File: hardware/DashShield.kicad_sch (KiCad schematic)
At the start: 121 parts, among them J001 PWR, J002 Data Logger, J101 CAN0, J202 CAN1, J3 Dash LEDs, J301 Steering Wheel, J601 GPIO, Q301 2N7002, Q302 2N7002, Q303 2N7002, Q501 2N7002, Q502 2N7002, Q503 2N7002, Q504 2N7002, Q505 2N7002, Q506 2N7002, U101 MCP2515-xST, U102 MCP2562-E-SN, U201 MCP2515-xST, U202 MCP2562-E-SN, U401 CAT24C256, U601 ADS1015IDGS, Y101 8MHz, Y201 8MHz

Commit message: feat: added pours & pass-through for CAN0&CAN1
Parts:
- added J102, J203: CAN0, Connector_Molex:Molex_Micro-Fit_3.0_43650-0315_1x03_P3.00mm_Vertical, symbol Connector_Generic:Conn_01x03
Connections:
- net CAN0 High: now also J102.1 (Pin_1)
- net CAN0 Low: now also J102.2 (Pin_2)
- net CAN0 Shield: now also J102.3 (Pin_3)
- net CAN1 High: now also J203.1 (Pin_1)
- net CAN1 Low: now also J203.2 (Pin_2)
- net CAN1 Shield: now also J203.3 (Pin_3)
- net FAST 2: now also J601.33 (Pin_33); no longer J601.32 (Pin_32)
- net FAST LED 0: now also J3.2 (Pin_2); no longer J3.8 (Pin_8)
- net FAST LED 1: now also J3.3 (Pin_3); no longer J3.4 (Pin_4)
- net FAST LED 2: now also J3.4 (Pin_4); no longer J3.3 (Pin_3)
- net GPIO19/PCM.FS: now also Q503.1 (G), R506.1; no longer Q502.1 (G), R504.1
- net GPIO26: now also Q502.1 (G), R504.1; no longer Q501.1 (G), R502.1
- net SLOW LED 1: now also J3.7 (Pin_7); no longer J3.2 (Pin_2)
- net SLOW LED 2: now also J3.8 (Pin_8); no longer J3.7 (Pin_7)
- removed net GPIO13/PWM1: J601.33 (Pin_33), Q503.1 (G), R506.1
- new net GPIO12/PWM0: J601.32 (Pin_32), Q501.1 (G), R502.1
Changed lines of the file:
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@@
     (stroke (width 0) (type default))
   )
+  (wire (pts (xy 369.57 29.718) (xy 381.508 29.718))
+    (stroke (width 0) (type default))
+  )
   (wire (pts (xy 20.32 72.39) (xy 54.61 72.39))
     (stroke (width 0) (type default))
@@
     (stroke (width 0) (type default))
   )
+  (wire (pts (xy 373.38 106.934) (xy 385.572 106.934))
+    (stroke (width 0) (type default))
+  )
   (wire (pts (xy 186.69 228.6) (xy 193.04 228.6))
     (stroke (width 0) (type default))
@@
     (stroke (width 0) (type default))
   )
+  (wire (pts (xy 369.57 32.258) (xy 381.508 32.258))
+    (stroke (width 0) (type default))
+  )
   (wire (pts (xy 321.31 58.42) (xy 330.2 58.42))
     (stroke (width 0) (type default))
@@
     (stroke (width 0) (type default))
   )
+  (wire (pts (xy 373.38 104.394) (xy 385.572 104.394))
+    (stroke (width 0) (type default))
+  )
   (wire (pts (xy 234.95 44.45) (xy 255.27 44.45))
     (stroke (width 0) (type default))
@@
     (stroke (width 0) (type default))
   )
+  (wire (pts (xy 373.38 101.854) (xy 385.572 101.854))
+    (stroke (width 0) (type default))
+  )
   (wire (pts (xy 187.96 69.85) (xy 195.58 69.85))
     (stroke (width 0) (type default))
@@
     (stroke (width 0) (type default))
   )
+  (wire (pts (xy 369.57 34.798) (xy 381.508 34.798))
+    (stroke (width 0) (type default))
+  )
   (wire (pts (xy 111.76 265.43) (xy 111.76 267.97))
     (stroke (width 0) (type default))
@@
     (effects (font (size 1.27 1.27)) (justify right bottom))
   )
-  (label "SLOW 2" (at 20.32 69.85 0) (fields_autoplaced)
+  (label "CAN1 High" (at 373.38 101.854 0) (fields_autoplaced)
+    (effects (font (size 1.27 1.27)) (justify left bottom))
+  )
+  (label "FAST 2" (at 20.32 69.85 0) (fields_autoplaced)
     (effects (font (size 1.27 1.27)) (justify left bottom))
   )
@@
     (effects (font (size 1.27 1.27)) (justify left bottom))
   )
+  (label "CAN0 High" (at 369.57 29.718 0) (fields_autoplaced)
+    (effects (font (size 1.27 1.27)) (justify left bottom))
+  )
   (label "CAN0 Low" (at 363.22 66.04 0) (fields_autoplaced)
     (effects (font (size 1.27 1.27)) (justify left bottom))
@@
     (effects (font (size 1.27 1.27)) (justify left bottom))
   )
-  (label "FAST 2" (at 107.95 67.31 180) (fields_autoplaced)
+  (label "SLOW 0" (at 107.95 67.31 180) (fields_autoplaced)
     (effects (font (size 1.27 1.27)) (justify right bottom))
   )
@@
     (effects (font (size 1.27 1.27)) (justify left bottom))
   )
+  (label "CAN1 Low" (at 373.38 104.394 0) (fields_autoplaced)
+    (effects (font (size 1.27 1.27)) (justify left bottom))
+  )
   (label "FAST 0" (at 119.38 104.14 0) (fields_autoplaced)
     (effects (font (size 1.27 1.27)) (justify left bottom))
   )
+  (label "CAN0 Low" (at 369.57 32.258 0) (fields_autoplaced)
+    (effects (font (size 1.27 1.27)) (justify left bottom))
+  )
+  (label "CAN1 Shield" (at 373.38 106.934 0) (fields_autoplaced)
+    (effects (font (size 1.27 1.27)) (justify left bottom))
+  )
   (label "GPIO22" (at 31.75 46.99 0) (fields_autoplaced)
     (effects (font (size 1.27 1.27)) (justify left bottom))
@@
     (effects (font (size 1.27 1.27)) (justify right bottom))
   )
-  (label "SLOW LED 2" (at 184.15 31.75 180) (fields_autoplaced)
+  (label "SLOW LED 1" (at 184.15 31.75 180) (fields_autoplaced)
     (effects (font (size 1.27 1.27)) (justify right bottom))
   )
@@
     (effects (font (size 1.27 1.27)) (justify left bottom))
   )
-  (label "SLOW 1" (at 20.32 72.39 0) (fields_autoplaced)
-    (effects (font (size 1.27 1.27)) (justify left bottom))
-  )
   (label "GPIO8{slash}SPI0.CE0" (at 234.95 41.91 0) (fields_autoplaced)
     (effects (font (size 1.27 1.27)) (justify left bottom))
@@
     (effects (font (size 1.27 1.27)) (justify right bottom))
   )
-  (label "FAST LED 1" (at 148.59 34.29 0) (fields_autoplaced)
+  (label "FAST LED 2" (at 148.59 34.29 0) (fields_autoplaced)
     (effects (font (size 1.27 1.27)) (justify left bottom))
   )
@@
     (effects (font (size 1.27 1.27)) (justify left bottom))
   )
-  (label "FAST LED 2" (at 148.59 31.75 0) (fields_autoplaced)
+  (label "FAST LED 1" (at 148.59 31.75 0) (fields_autoplaced)
     (effects (font (size 1.27 1.27)) (justify left bottom))
   )
@@
     (effects (font (size 1.27 1.27)) (justify left bottom))
   )
-  (label "FAST LED 0" (at 184.15 34.29 180) (fields_autoplaced)
+  (label "SLOW LED 2" (at 184.15 34.29 180) (fields_autoplaced)
     (effects (font (size 1.27 1.27)) (justify right bottom))
   )
@@
     (effects (font (size 1.27 1.27)) (justify right bottom))
   )
-  (label "SLOW 0" (at 20.32 74.93 0) (fields_autoplaced)
+  (label "SLOW 1" (at 20.32 74.93 0) (fields_autoplaced)
     (effects (font (size 1.27 1.27)) (justify left bottom))
   )
@@
     (effects (font (size 1.27 1.27)) (justify left bottom))
   )
+  (label "SLOW 2" (at 20.32 72.39 0) (fields_autoplaced)
+    (effects (font (size 1.27 1.27)) (justify left bottom))
+  )
   (label "Wheel Slip Adjust Dial" (at 346.71 209.55 0) (fields_autoplaced)
     (effects (font (size 1.27 1.27)) (justify left bottom))
@@
     (effects (font (size 1.27 1.27)) (justify left bottom))
   )
+  (label "CAN0 Shield" (at 369.57 34.798 0) (fields_autoplaced)
+    (effects (font (size 1.27 1.27)) (justify left bottom))
+  )
   (label "TC Power Adjust" (at 57.15 115.57 0) (fields_autoplaced)
     (effects (font (size 1.27 1.27)) (justify left bottom))
@@
     (effects (font (size 1.27 1.27)) (justify left bottom))
   )
-  (label "SLOW LED 1" (at 148.59 29.21 0) (fields_autoplaced)
+  (label "FAST LED 0" (at 148.59 29.21 0) (fields_autoplaced)
     (effects (font (size 1.27 1.27)) (justify left bottom))
   )
@@
     )
   )
+  (symbol (lib_id "Connector_Generic:Conn_01x03") (at 386.588 32.258 0) (unit 1)
+    (in_bom yes) (on_board yes) (dnp no) (fields_autoplaced)
+    (property "Reference" "J102" (at 388.62 30.988 0)
+      (effects (font (size 1.27 1.27)) (justify left))
+    )
+    (property "Value" "CAN0" (at 388.62 33.528 0)
+      (effects (font (size 1.27 1.27)) (justify left))
+    )
+    (property "Footprint" "Connector_Molex:Molex_Micro-Fit_3.0_43650-0315_1x03_P3.00mm_Vertical" (at 386.588 32.258 0)
+      (effects (font (size 1.27 1.27)) hide)
+    )
+    (property "Datasheet" "~" (at 386.588 32.258 0)
+      (effects (font (size 1.27 1.27)) hide)
+    )
+    (pin "1")
+    (pin "2")
+    (pin "3")
+    (instances
+      (project "DashShield"
+        (path "/e63e39d7-6ac0-4ffd-8aa3-1841a4541b55"
+          (reference "J102") (unit 1)
+        )
+      )
+    )
+  )
   (symbol (lib_id "Device:R") (at 245.11 139.7 270) (unit 1)
     (in_bom yes) (on_board yes) (dnp no)
@@
         )
       )
+    )
+  )
+  (symbol (lib_id "Connector_Generic:Conn_01x03") (at 390.652 104.394 0) (unit 1)
+    (in_bom yes) (on_board yes) (dnp no) (fields_autoplaced)
+    (property "Reference" "J203" (at 393.192 103.124 0)
+      (effects (font (size 1.27 1.27)) (justify left))
+    )
+    (property "Value" "CAN0" (at 393.192 105.664 0)
+      (effects (font (size 1.27 1.27)) (justify left))
+    )
+    (property "Footprint" "Connector_Molex:Molex_Micro-Fit_3.0_43650-0315_1x03_P3.00mm_Vertical" (at 390.652 104.394 0)
+      (effects (font (size 1.27 1.27)) hide)
+    )
+    (property "Datasheet" "~" (at 390.652 104.394 0)
+      (effects (font (size 1.27 1.27)) hide)
+    )
+    (pin "1")
+    (pin "2")
+    (pin "3")
+    (instances
+      (project "DashShield"
+        (path "/e63e39d7-6ac0-4ffd-8aa3-1841a4541b55"
+          (reference "J203") (unit 1)
+        )
+      )

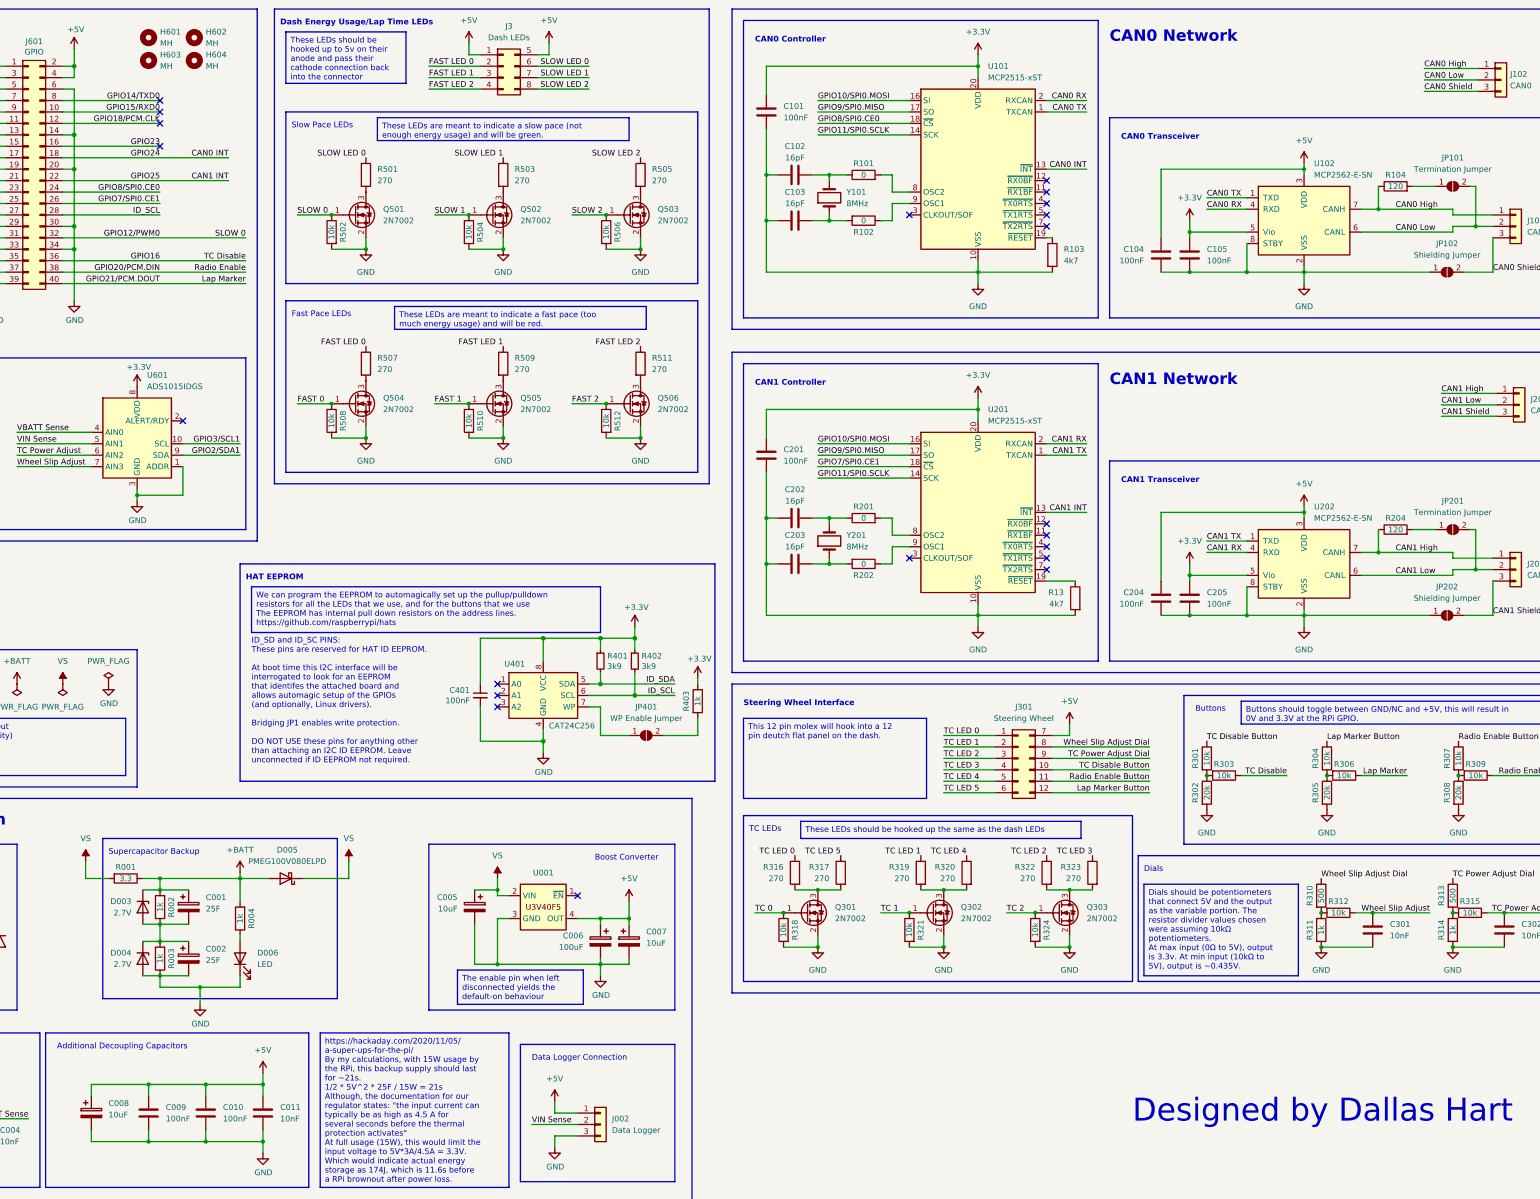
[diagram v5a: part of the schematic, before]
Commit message: chore: add all LCSC parts and update footprints
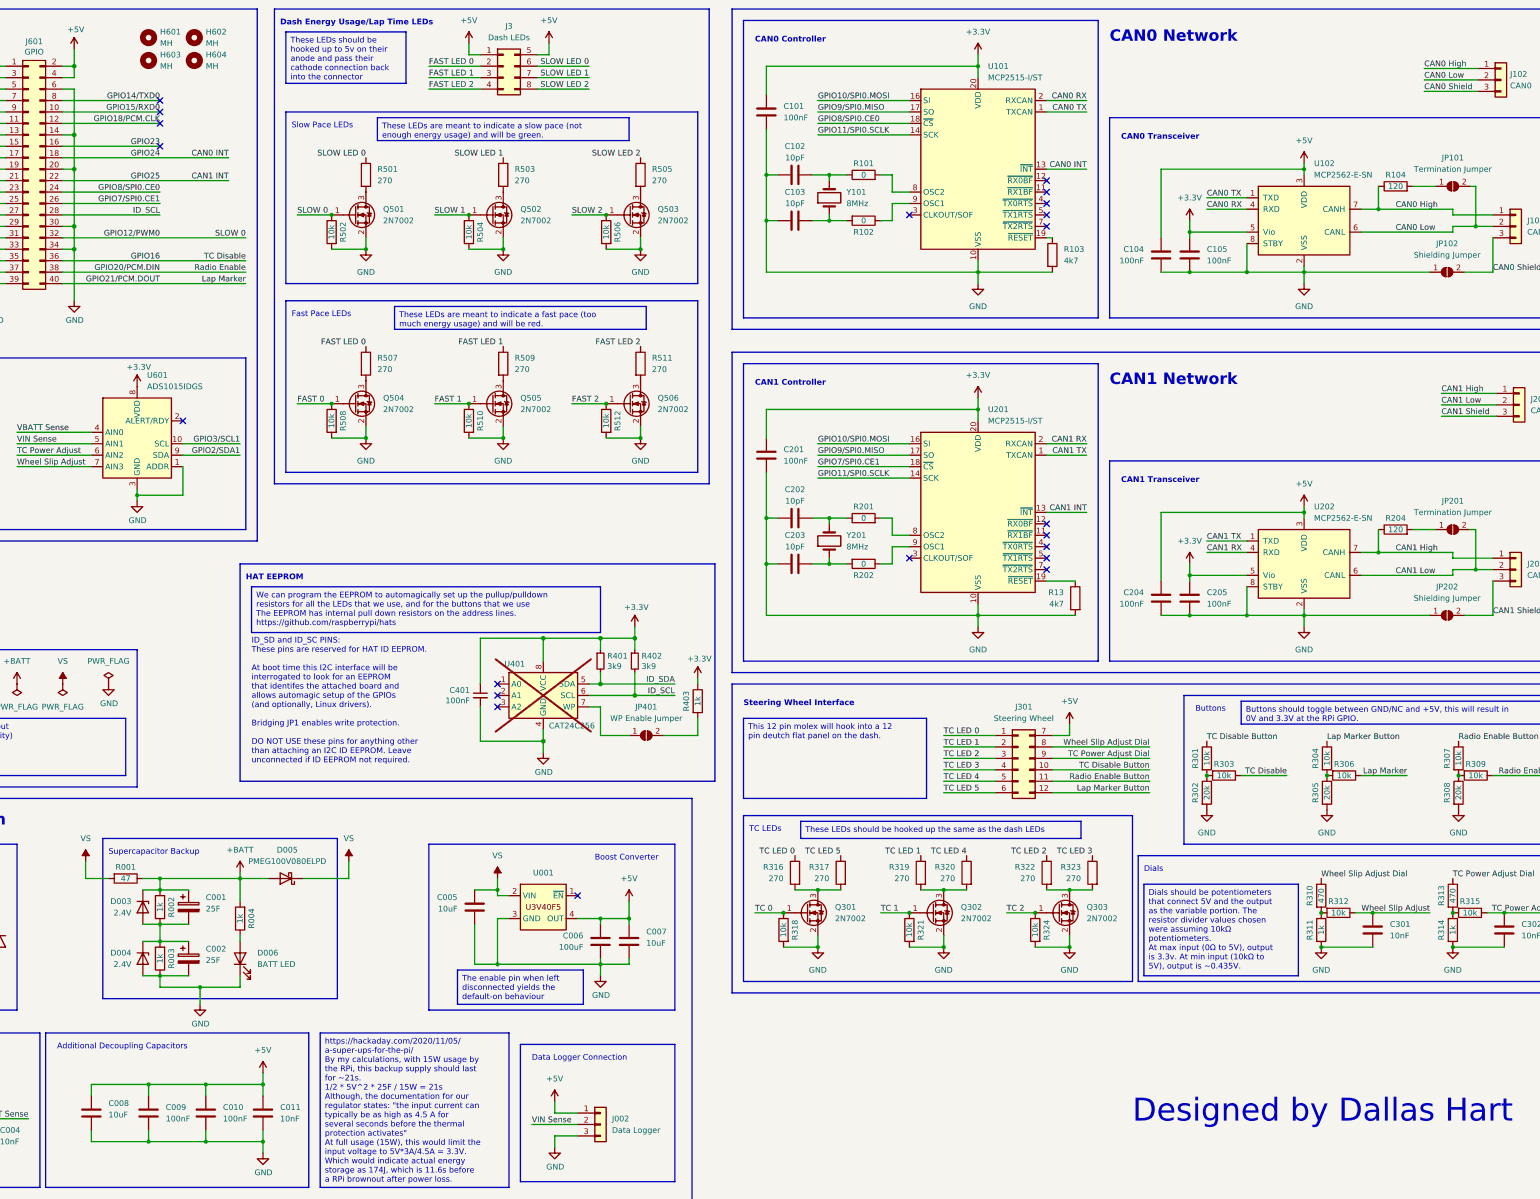
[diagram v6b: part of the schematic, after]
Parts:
- C003, C004, C011, C301, C302, C602: LCSC (none) -> C57112
- C005, C007, C008: footprint Capacitor_THT:CP_Radial_D5.0mm_P2.50mm -> Capacitor_SMD:C_0603_1608Metric; symbol Device:C_Polarized -> Device:C; LCSC (none) -> C19702
- C006: footprint Capacitor_THT:CP_Radial_D5.0mm_P2.50mm -> Capacitor_SMD:C_1206_3216Metric; symbol Device:C_Polarized -> Device:C; LCSC (none) -> C15008
- C009, C010, C101, C104, C105, C201, C204, C205, C401, C601: LCSC (none) -> C14663
- C102, C103, C202, C203: value 16pF -> 10pF; LCSC (none) -> C1634
- D001, D005: LCSC (none) -> C458185
- D002: footprint Diode_SMD:D_SMA -> Diode_SMD:D_SMB; LCSC (none) -> C2940070
- D003, D004: value 2.7V -> 2.4V; LCSC (none) -> C411194
- D006: value LED -> BATT LED; LCSC (none) -> C72038
- J601: now left out of the parts list
- Q301, Q302, Q303, Q501, Q502, Q503, Q504, Q505, Q506: LCSC (none) -> C8545
- R001: value 3.3 -> 47; footprint Resistor_SMD:R_0603_1608Metric -> Resistor_SMD:R_2512_6332Metric; LCSC (none) -> C2913007
- R002, R003, R004, R311, R314, R403: LCSC (none) -> C21190
- R005, R007, R301, R303, R304, R306, R307, R309, R312, R315, R318, R321, R324, R502, R504, R506, R508, R510, R512: LCSC (none) -> C25804
- R006, R008, R302, R305, R308: LCSC (none) -> C4184
- R101, R102, R201, R202: LCSC (none) -> C21189
- R103, R13: LCSC (none) -> C23162
- R104, R204: LCSC (none) -> C22787
- R310, R313: value 500 -> 470; LCSC (none) -> C23179
- R316, R317, R319, R320, R322, R323, R501, R503, R505, R507, R509, R511: LCSC (none) -> C22966
- R401, R402: LCSC (none) -> C23018
- U101, U201: value MCP2515-xST -> MCP2515-I/ST; LCSC (none) -> C15193
- U102, U202: LCSC (none) -> C191417
- U401: LCSC (none) -> C79987; now not fitted
- U601: LCSC (none) -> C193969
- Y101, Y201: footprint Crystal:Crystal_C38-LF_D3.0mm_L8.0mm_Vertical -> Crystal:Crystal_SMD_Abracon_ABM3B-4Pin_5.0x3.2mm; LCSC (none) -> C276420
